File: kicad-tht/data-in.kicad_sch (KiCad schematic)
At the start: 37 parts, among them SW0 SW_SPDT, SW1 SW_SPDT, SW2 SW_SPDT, SW3 SW_SPDT, SW4 SW_SPDT, SW5 SW_SPDT, SW6 SW_SPDT, SW7 SW_SPDT, SW8 SW_SPDT, SW9 SW_SPDT

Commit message: file updates
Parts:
- removed JP1: Jumper, Connector_PinHeader_2.54mm:PinHeader_1x02_P2.54mm_Vertical, symbol Jumper:Jumper_2_Bridged
- R1, R10, R2, R3, R4, R5, R6, R7, R8, R9: value 10K -> 100K
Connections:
- net VIO_2V5: now also SW0.3 (C), SW1.3 (C), SW2.3 (C), SW3.3 (C), SW4.3 (C), SW5.3 (C), SW6.3 (C), SW7.3 (C), SW8.3 (C), SW9.3 (C)
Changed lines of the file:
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@@
-    (stroke (width 0) (type default) (color 0 0 0 0))
-  )
-  (wire (pts (xy 163.83 38.1) (xy 171.45 38.1))
     (stroke (width 0) (type default) (color 0 0 0 0))
   )
@@
     (stroke (width 0) (type default) (color 0 0 0 0))
   )
-  (wire (pts (xy 149.86 38.1) (xy 153.67 38.1))
+  (wire (pts (xy 160.02 38.1) (xy 171.45 38.1))
     (stroke (width 0) (type default) (color 0 0 0 0))
   )
@@
     )
   )
-  (global_label "VIO_2V5" (shape input) (at 149.86 38.1 180) (fields_autoplaced)
+  (global_label "VIO_2V5" (shape input) (at 160.02 38.1 180) (fields_autoplaced)
     (effects (font (size 1.27 1.27)) (justify right))
-    (property "Intersheet References" "${INTERSHEET_REFS}" (id 0) (at 139.9479 38.0206 0)
+    (property "Intersheet References" "${INTERSHEET_REFS}" (id 0) (at 150.1079 38.0206 0)
       (effects (font (size 1.27 1.27)) (justify right) hide)
     )
@@
     (in_bom yes) (on_board yes)
     (property "Reference" "R2" (id 0) (at 176.53 66.04 90))
-    (property "Value" "10K" (id 1) (at 181.61 66.04 90))
+    (property "Value" "100K" (id 1) (at 181.61 66.04 90))
     (property "Footprint" "Resistor_SMD:R_0402_1005Metric" (id 2) (at 179.07 66.04 0)
       (effects (font (size 1.27 1.27)) hide)
@@
     (in_bom yes) (on_board yes)
     (property "Reference" "R5" (id 0) (at 207.01 66.04 90))
-    (property "Value" "10K" (id 1) (at 212.09 66.04 90))
+    (property "Value" "100K" (id 1) (at 212.09 66.04 90))
     (property "Footprint" "Resistor_SMD:R_0402_1005Metric" (id 2) (at 209.55 66.04 0)
       (effects (font (size 1.27 1.27)) hide)
@@
     (in_bom yes) (on_board yes)
     (property "Reference" "R10" (id 0) (at 257.81 66.04 90))
-    (property "Value" "10K" (id 1) (at 262.89 66.04 90))
+    (property "Value" "100K" (id 1) (at 262.89 66.04 90))
     (property "Footprint" "Resistor_SMD:R_0402_1005Metric" (id 2) (at 260.35 66.04 0)
       (effects (font (size 1.27 1.27)) hide)
@@
     (in_bom yes) (on_board yes)
     (property "Reference" "R8" (id 0) (at 237.49 66.04 90))
-    (property "Value" "10K" (id 1) (at 242.57 66.04 90))
+    (property "Value" "100K" (id 1) (at 242.57 66.04 90))
     (property "Footprint" "Resistor_SMD:R_0402_1005Metric" (id 2) (at 240.03 66.04 0)
       (effects (font (size 1.27 1.27)) hide)
@@
     (in_bom yes) (on_board yes)
     (property "Reference" "R9" (id 0) (at 247.65 66.04 90))
-    (property "Value" "10K" (id 1) (at 252.73 66.04 90))
+    (property "Value" "100K" (id 1) (at 252.73 66.04 90))
     (property "Footprint" "Resistor_SMD:R_0402_1005Metric" (id 2) (at 250.19 66.04 0)
       (effects (font (size 1.27 1.27)) hide)
@@
     (in_bom yes) (on_board yes)
     (property "Reference" "R6" (id 0) (at 217.17 66.04 90))
-    (property "Value" "10K" (id 1) (at 222.25 66.04 90))
+    (property "Value" "100K" (id 1) (at 222.25 66.04 90))
     (property "Footprint" "Resistor_SMD:R_0402_1005Metric" (id 2) (at 219.71 66.04 0)
       (effects (font (size 1.27 1.27)) hide)
@@
     (in_bom yes) (on_board yes)
     (property "Reference" "R1" (id 0) (at 166.37 66.04 90))
-    (property "Value" "10K" (id 1) (at 171.45 66.04 90))
+    (property "Value" "100K" (id 1) (at 171.45 66.04 90))
     (property "Footprint" "Resistor_SMD:R_0402_1005Metric" (id 2) (at 168.91 66.04 0)
       (effects (font (size 1.27 1.27)) hide)
@@
     (pin "3")
   )
-  (symbol (lib_id "Jumper:Jumper_2_Bridged") (at 158.75 38.1 180) (unit 1)
-    (in_bom yes) (on_board yes)
-    (property "Reference" "JP1" (id 0) (at 157.48 35.56 0)
-      (effects (font (size 1.27 1.27)) (justify right))
-    )
-    (property "Value" "Jumper" (id 1) (at 154.94 41.91 0)
-      (effects (font (size 1.27 1.27)) (justify right))
-    )
-    (property "Footprint" "Connector_PinHeader_2.54mm:PinHeader_1x02_P2.54mm_Vertical" (id 2) (at 158.75 38.1 0)
-      (effects (font (size 1.27 1.27)) hide)
-    )
-    (property "Datasheet" "~" (id 3) (at 158.75 38.1 0)
-      (effects (font (size 1.27 1.27)) hide)
-    )
-    (pin "1")
-    (pin "2")
-  )
   (symbol (lib_id "Device:R_Small") (at 189.23 66.04 180) (unit 1)
     (in_bom yes) (on_board yes)
     (property "Reference" "R3" (id 0) (at 186.69 66.04 90))
-    (property "Value" "10K" (id 1) (at 191.77 66.04 90))
+    (property "Value" "100K" (id 1) (at 191.77 66.04 90))
     (property "Footprint" "Resistor_SMD:R_0402_1005Metric" (id 2) (at 189.23 66.04 0)
       (effects (font (size 1.27 1.27)) hide)
@@
     (in_bom yes) (on_board yes)
     (property "Reference" "R7" (id 0) (at 227.33 66.04 90))
-    (property "Value" "10K" (id 1) (at 232.41 66.04 90))
+    (property "Value" "100K" (id 1) (at 232.41 66.04 90))
     (property "Footprint" "Resistor_SMD:R_0402_1005Metric" (id 2) (at 229.87 66.04 0)
       (effects (font (size 1.27 1.27)) hide)
@@
     (in_bom yes) (on_board yes)
     (property "Reference" "R4" (id 0) (at 196.85 66.04 90))
-    (property "Value" "10K" (id 1) (at 201.93 66.04 90))
+    (property "Value" "100K" (id 1) (at 201.93 66.04 90))
     (property "Footprint" "Resistor_SMD:R_0402_1005Metric" (id 2) (at 199.39 66.04 0)
       (effects (font (size 1.27 1.27)) hide)

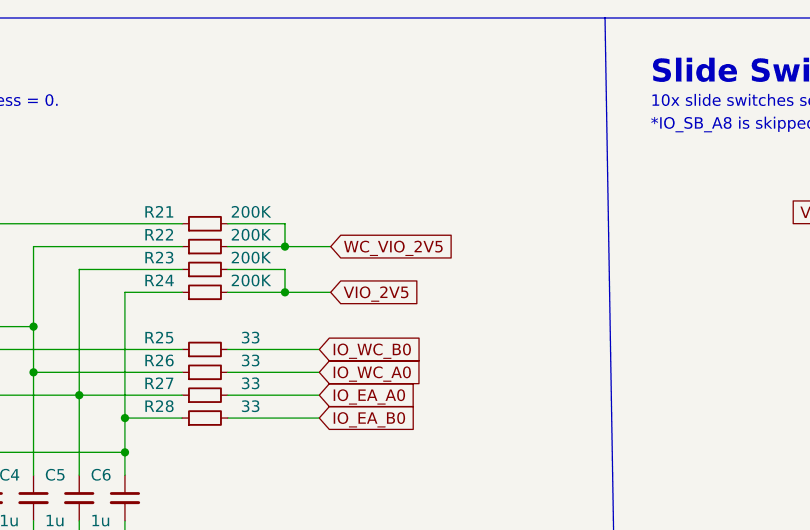
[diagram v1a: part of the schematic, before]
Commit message: New THT PCB v1.1 updates J1 level translation IC
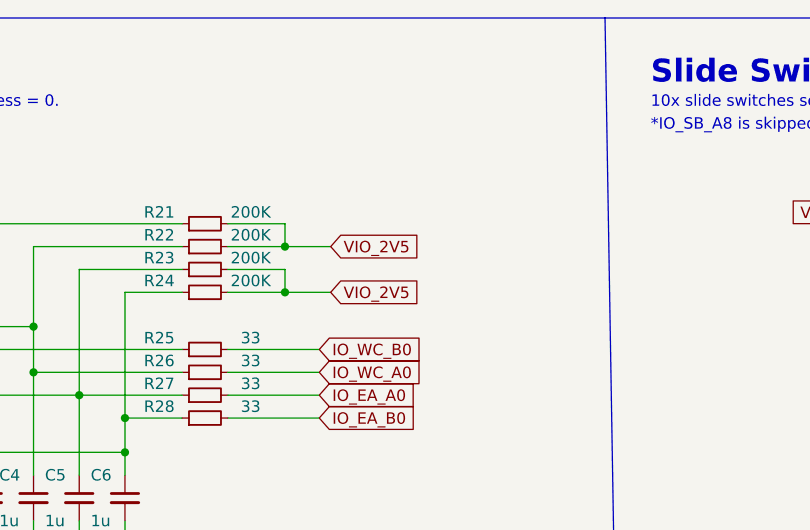
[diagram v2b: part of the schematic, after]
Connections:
- net WC_VIO_2V5 is gone; now on net VIO_2V5: R21.2, R22.2
